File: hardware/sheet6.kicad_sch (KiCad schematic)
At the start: 9 parts

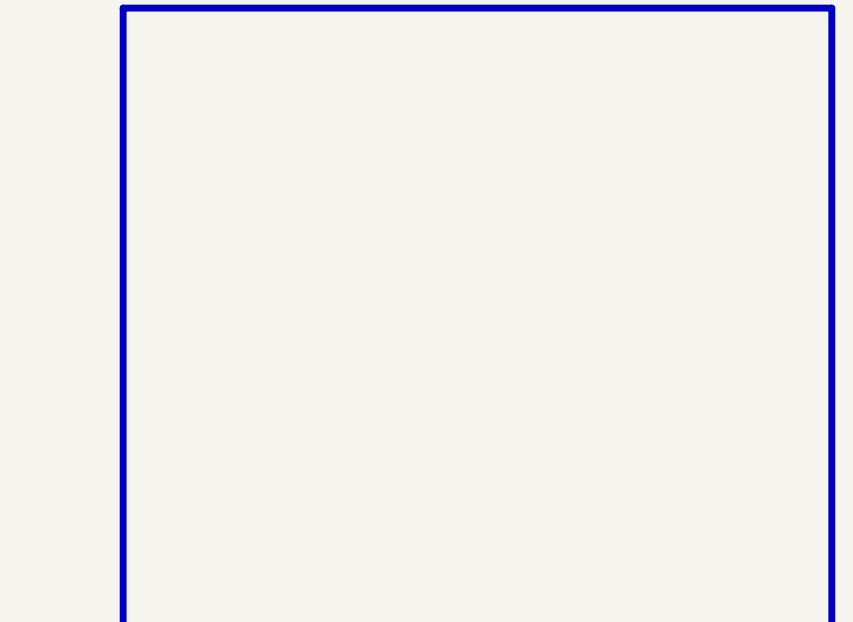
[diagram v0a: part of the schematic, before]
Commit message: hardware(feat): add lm75bd temperature sensor on i2c1 (#4)
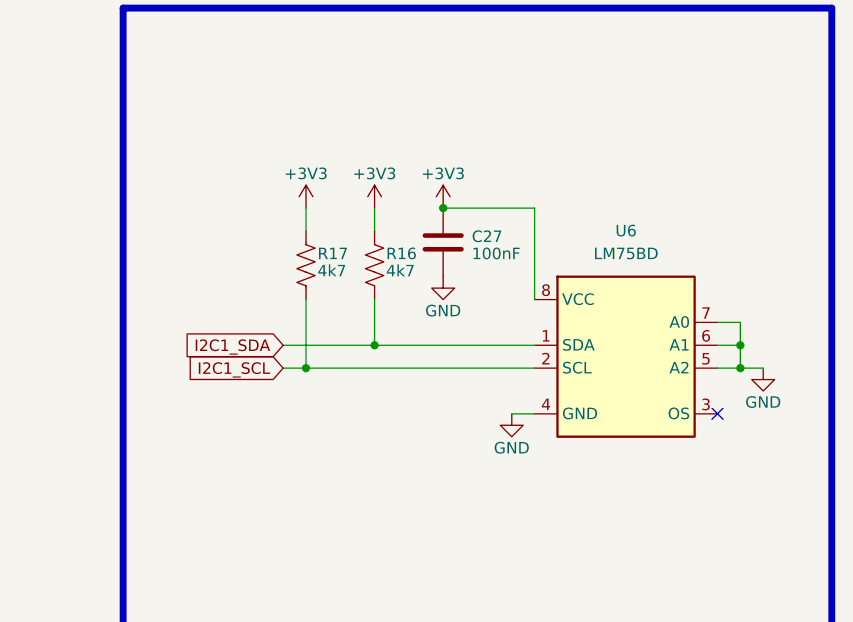
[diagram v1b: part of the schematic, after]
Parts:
- added C27: 100nF, 02_capacitors:C_0603_1608Metric, symbol 02_capacitors:CAP_100nF-50V-10%-X7R-0603
- added R16, R17: 4k7, 01_resistors:R_0603_1608Metric, symbol 01_resistors:RES_4.7K-0.1W-1%-0603
- added U6: LM75BD, 06_ics:SOIC-8_3.9x4.9mm_P1.27mm, symbol 06_ics:IC-SNS_LM75BD
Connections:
- net +3V3: now also C27.1, R16.1, R17.1, U6.8 (VCC)
- net GND: now also C27.2, U6.4 (GND), U6.5 (A2), U6.6 (A1), U6.7 (A0)
- new net I2C1_SCL: R17.2, U6.2 (SCL)
- new net I2C1_SDA: R16.2, U6.1 (SDA)
- no-connect marks 0 -> 1

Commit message: hardware(feat): add 16x2 lcd with pcf8574 on i2c1 (#5)
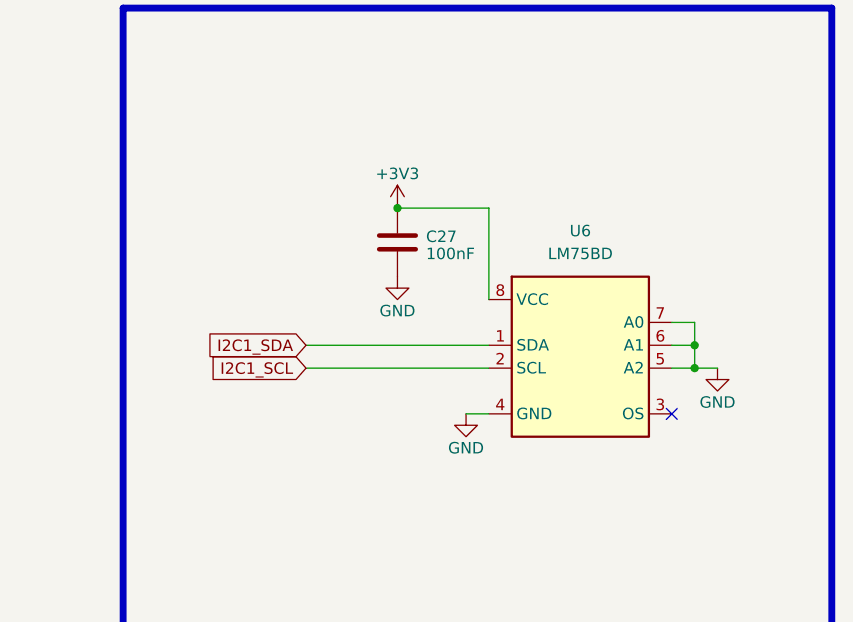
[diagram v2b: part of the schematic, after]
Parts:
- removed R16, R17: 4k7, 01_resistors:R_0603_1608Metric, symbol 01_resistors:RES_4.7K-0.1W-1%-0603
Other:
- moved on the sheet: C27, U6
